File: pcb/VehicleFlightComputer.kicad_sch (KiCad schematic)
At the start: 65 parts, among them J1 FFC2B28-24-G, J3 USB_C_Receptacle, J4 Debug, Q1 S8050, SW1 B3U-1000P, U1 STM32H533VET6, U2 LIS2MDL, U3 LSM6DSV32X, U4 MCP2221A-I/ST, U5 AP2112K-3.3

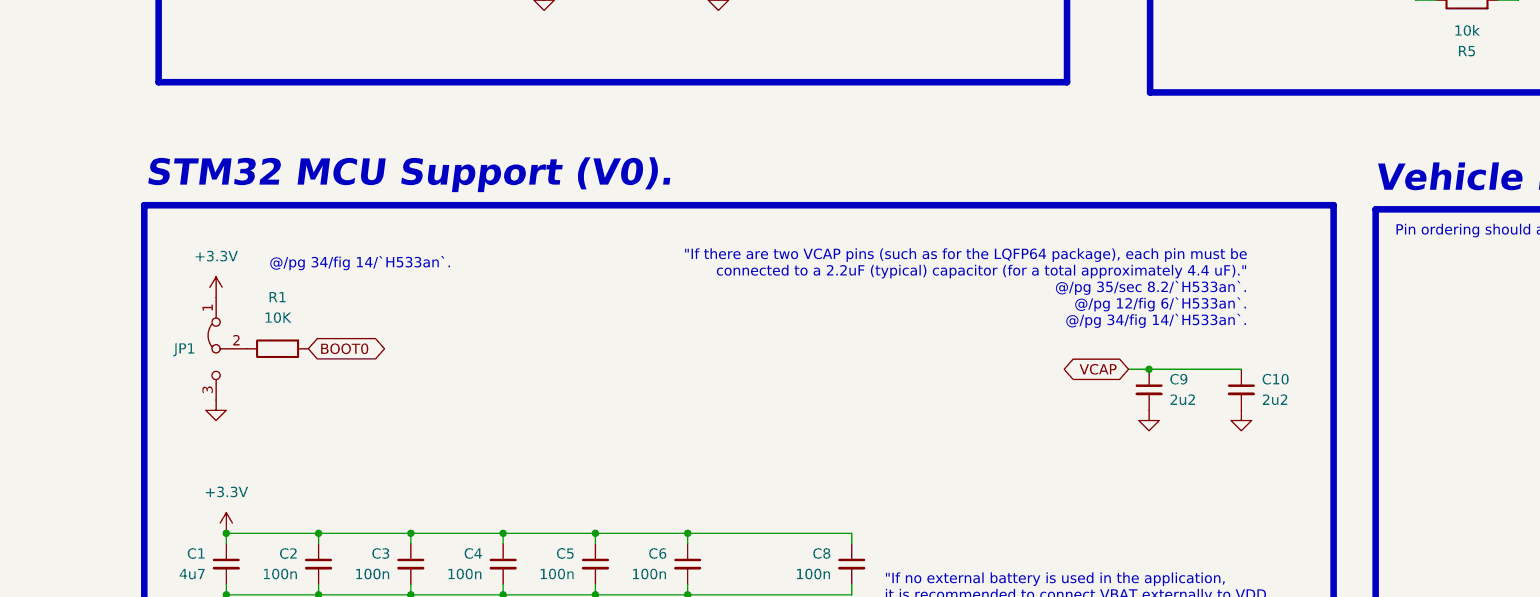
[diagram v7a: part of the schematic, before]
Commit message: `STM32 MCU Support (V1 : Smaller BOOT0 setting).`
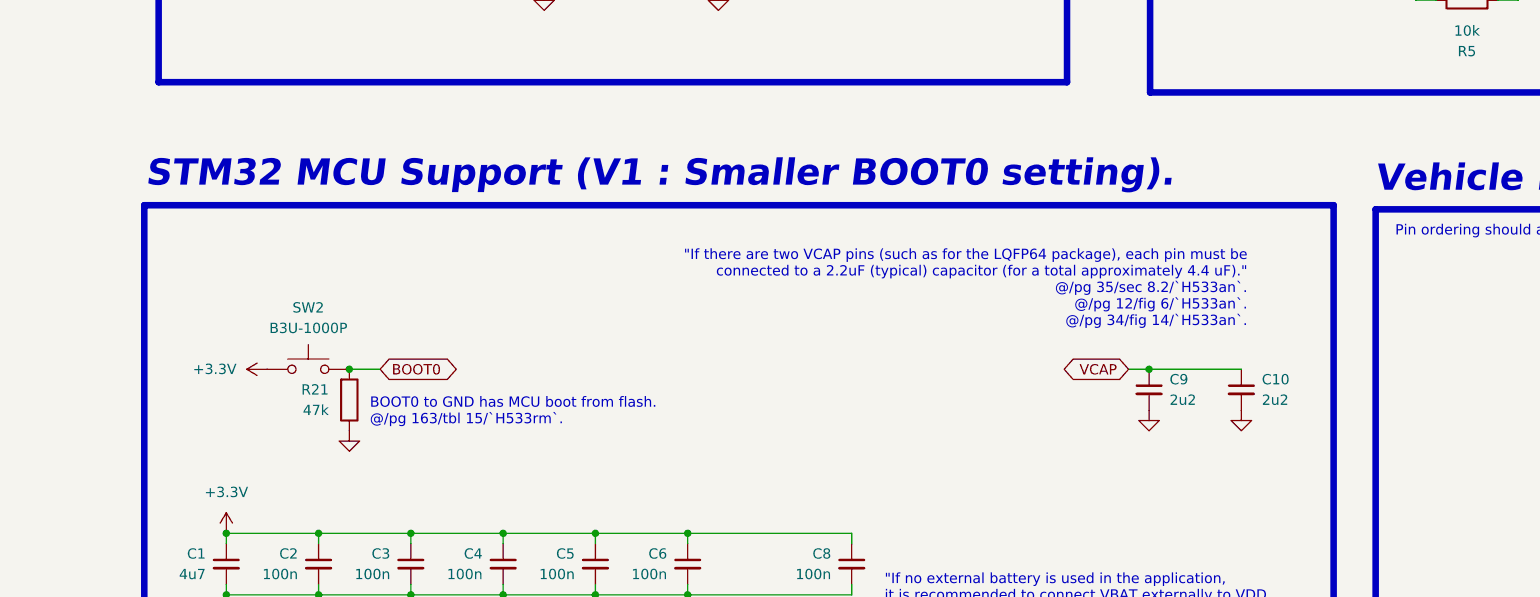
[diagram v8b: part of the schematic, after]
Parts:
- removed JP1: Jumper_3_Bridged12, Connector_PinHeader_2.54mm:PinHeader_1x03_P2.54mm_Vertical, symbol Jumper:Jumper_3_Bridged12
- removed R1: 10K, Resistor_SMD:R_1206_3216Metric_Pad1.30x1.75mm_HandSolder, symbol Device:R
- added R21: 47k, Resistor_SMD:R_1206_3216Metric_Pad1.30x1.75mm_HandSolder, symbol Device:R
- added SW2: B3U-1000P, Button_Switch_SMD:SW_SPST_B3U-1000P, symbol Switch:SW_Push
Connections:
- net +3.3V: now also SW2.1
- net BOOT0: now also R21.2, SW2.2
- net GND: now also R21.1
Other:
- note added: "BOOT0 to GND has MCU boot from flash. @/pg 163/tbl 15/`H533rm`."
- note added: "STM32 MCU Support (V1 : Smaller BOOT0 setting)."
- note removed: "@/pg 34/fig 14/`H533an`."
- note removed: "STM32 MCU Support (V0)."
